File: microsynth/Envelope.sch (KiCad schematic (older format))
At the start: 42 parts, among them Q3 BC548, SW18-ENV-TO-VCF1 SW_SPDT, SW19-ENV-TO-VCO1 SW_SPDT, SW20-ENV-TO-KEYB1 SW_SPDT, SW7 SW_SPDT, SW8 SW_DPTT_SELECTOR-Switch, SW9 TRIGGER, U10 LM741, U3 4011, U4 4016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

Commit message: Change switch footprints
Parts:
- SW8, SW9: footprint Buttons_Switches_ThroughHole:DP3T_Toggle -> Buttons_Switches_ThroughHole:L203011MS02Q
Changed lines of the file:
@@
 F 0 "SW9" H 7900 4800 50  0000 L CNN
 F 1 "TRIGGER" H 7900 4700 50  0000 L CNN
-F 2 "Buttons_Switches_ThroughHole:DP3T_Toggle" H 7700 4800 50  0001 C CNN
+F 2 "Buttons_Switches_ThroughHole:L203011MS02Q" H 7700 4800 50  0001 C CNN
 F 3 "" H 7700 4800 50  0001 C CNN
 	1    7700 4800
@@
 F 0 "SW8" H 3200 3750 50  0000 L CNN
 F 1 "SW_DPTT_SELECTOR-Switch" H 3200 3650 50  0000 L CNN
-F 2 "Buttons_Switches_ThroughHole:DP3T_Toggle" H 2950 3550 50  0001 C CNN
+F 2 "Buttons_Switches_ThroughHole:L203011MS02Q" H 2950 3550 50  0001 C CNN
 F 3 "http://switches-connectors-custom.cwind.com/Asset/G-1128S-1110_2D%20DRAWING.pdf" H 2950 3550 50  0001 C CNN
 F 4 "Sustain" H 3200 3550 50  0000 L CNN "Label"
@@
 F 0 "SW8" H 3200 3650 50  0000 L CNN
 F 1 "SW_DPTT_SELECTOR-Switch" H 3200 3550 50  0000 L CNN
-F 2 "Buttons_Switches_ThroughHole:DP3T_Toggle" H 2950 3650 50  0001 C CNN
+F 2 "Buttons_Switches_ThroughHole:L203011MS02Q" H 2950 3650 50  0001 C CNN
 F 3 "http://switches-connectors-custom.cwind.com/Asset/G-1128S-1110_2D%20DRAWING.pdf" H 2950 3650 50  0001 C CNN
 	1    2950 3650

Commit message: Layout...-7
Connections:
- net +VSW: now also SW8.3; no longer SW8.7
- net TO_VCA_R136: now also SW8.4; no longer SW8.8
- net at R61.2, U4.5: now also SW8.6, SW8.8; no longer SW8.2, SW8.4
- net at U8.10, U8.12: now also SW8.7; no longer SW8.3
- net at C10.2, C9.2, D5.1 (K)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: now also SW8.5; no longer SW8.1
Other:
- moved on the sheet: SW8A, SW8B
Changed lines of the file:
@@
 L Switch:SW_DPTT_SELECTOR-Switch SW8
 U 2 1 5F2DFAB2
-P 2950 3550
-F 0 "SW8" H 3200 3750 50  0000 L CNN
-F 1 "SW_DPTT_SELECTOR-Switch" H 3200 3650 50  0000 L CNN
-F 2 "Buttons_Switches_ThroughHole:L203011MS02Q" H 2950 3550 50  0001 C CNN
-F 3 "http://switches-connectors-custom.cwind.com/Asset/G-1128S-1110_2D%20DRAWING.pdf" H 2950 3550 50  0001 C CNN
-F 4 "Sustain" H 3200 3550 50  0000 L CNN "Label"
-	2    2950 3550
-	1    0    0    -1
+P 2950 3650
+F 0 "SW8" H 3200 3850 50  0000 L CNN
+F 1 "SW_DPTT_SELECTOR-Switch" H 3200 3750 50  0000 L CNN
+F 2 "Buttons_Switches_ThroughHole:L203011MS02Q" H 2950 3650 50  0001 C CNN
+F 3 "http://switches-connectors-custom.cwind.com/Asset/G-1128S-1110_2D%20DRAWING.pdf" H 2950 3650 50  0001 C CNN
+F 4 "Sustain" H 3200 3650 50  0000 L CNN "Label"
+	2    2950 3650
+	1    0    0    1
 $EndComp
 $Comp
 L Switch:SW_DPTT_SELECTOR-Switch SW8
 U 1 1 5F2DEA06
-P 2950 3650
-F 0 "SW8" H 3200 3650 50  0000 L CNN
-F 1 "SW_DPTT_SELECTOR-Switch" H 3200 3550 50  0000 L CNN
-F 2 "Buttons_Switches_ThroughHole:L203011MS02Q" H 2950 3650 50  0001 C CNN
-F 3 "http://switches-connectors-custom.cwind.com/Asset/G-1128S-1110_2D%20DRAWING.pdf" H 2950 3650 50  0001 C CNN
-	1    2950 3650
-	1    0    0    -1
+P 2950 3550
+F 0 "SW8" H 3200 3550 50  0000 L CNN
+F 1 "SW_DPTT_SELECTOR-Switch" H 3200 3450 50  0000 L CNN
+F 2 "Buttons_Switches_ThroughHole:L203011MS02Q" H 2950 3550 50  0001 C CNN
+F 3 "http://switches-connectors-custom.cwind.com/Asset/G-1128S-1110_2D%20DRAWING.pdf" H 2950 3550 50  0001 C CNN
+	1    2950 3550
+	1    0    0    1
 $EndComp
 Wire Wire Line

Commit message: Layout...-3
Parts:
- SW8: value SW_DPTT_SELECTOR-Switch -> SUSTAIN
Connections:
- net +VSW: now also SW8.7; no longer SW8.3
- net TO_D3: now also SW9.6; no longer SW9.3
- net TO_VCA_R136: now also SW8.8; no longer SW8.4
- net at R61.2, U4.5: now also SW8.2, SW8.4; no longer SW8.6, SW8.8
- net at U8.10, U8.12: now also SW8.3; no longer SW8.7
- net at C10.2, C9.2, D5.1 (K)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: now also SW8.1; no longer SW8.5
- net at C13.2, U3.10, U3.12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: now also SW9.7; no longer SW9.2
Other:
- moved on the sheet: SW8A, SW8B
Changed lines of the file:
@@
 	8850 4300 8800 4300
 $Comp
-L power:-VSW #PWR0182
+L power:-VSW #PWR?
 U 1 1 5E64C648
 P 8850 4800
-F 0 "#PWR0182" H 8850 4900 50  0001 C CNN
+F 0 "#PWR?" H 8850 4900 50  0001 C CNN
 F 1 "-VSW" H 8865 4973 50  0000 C CNN
 F 2 "" H 8850 4800 50  0001 C CNN
@@
 $EndComp
 $Comp
-L power:GND #PWR0183
+L power:GND #PWR?
 U 1 1 5E652014
 P 5600 3600
-F 0 "#PWR0183" H 5600 3350 50  0001 C CNN
+F 0 "#PWR?" H 5600 3350 50  0001 C CNN
 F 1 "GND" H 5605 3427 50  0000 C CNN
 F 2 "" H 5600 3600 50  0001 C CNN
@@
 Connection ~ 6300 4250
 $Comp
-L power:GND #PWR0184
+L power:GND #PWR?
 U 1 1 5E65990E
 P 5600 5000
-F 0 "#PWR0184" H 5600 4750 50  0001 C CNN
+F 0 "#PWR?" H 5600 4750 50  0001 C CNN
 F 1 "GND" H 5605 4827 50  0000 C CNN
 F 2 "" H 5600 5000 50  0001 C CNN
@@
 	5600 4750 5650 4750
 $Comp
-L power:-VSW #PWR0185
+L power:-VSW #PWR?
 U 1 1 5E65BC6F
 P 6650 4900
-F 0 "#PWR0185" H 6650 5000 50  0001 C CNN
+F 0 "#PWR?" H 6650 5000 50  0001 C CNN
 F 1 "-VSW" H 6665 5073 50  0000 C CNN
 F 2 "" H 6650 4900 50  0001 C CNN
@@
 	1300 3100 1400 3100
 $Comp
-L power:-VSW #PWR0186
+L power:-VSW #PWR?
 U 1 1 5E66382E
 P 1300 3650
-F 0 "#PWR0186" H 1300 3750 50  0001 C CNN
+F 0 "#PWR?" H 1300 3750 50  0001 C CNN
 F 1 "-VSW" H 1315 3823 50  0000 C CNN
 F 2 "" H 1300 3650 50  0001 C CNN
@@
 	1300 3650 1300 3550
 $Comp
-L power:-VSW #PWR0187
+L power:-VSW #PWR?
 U 1 1 5E666239
 P 5150 5150
-F 0 "#PWR0187" H 5150 5250 50  0001 C CNN
+F 0 "#PWR?" H 5150 5250 50  0001 C CNN
 F 1 "-VSW" H 5165 5323 50  0000 C CNN
 F 2 "" H 5150 5150 50  0001 C CNN
@@
 	3850 3050 3850 3300
 $Comp
-L power:+VSW #PWR0188
+L power:+VSW #PWR?
 U 1 1 5E66EFC8
 P 4350 3050
-F 0 "#PWR0188" H 4350 2900 50  0001 C CNN
+F 0 "#PWR?" H 4350 2900 50  0001 C CNN
 F 1 "+VSW" H 4365 3223 50  0000 C CNN
 F 2 "" H 4350 3050 50  0001 C CNN
@@
 $EndComp
 $Comp
-L power:-VSW #PWR0189
+L power:-VSW #PWR?
 U 1 1 5E6A252E
 P 1300 2350
-F 0 "#PWR0189" H 1300 2450 50  0001 C CNN
+F 0 "#PWR?" H 1300 2450 50  0001 C CNN
 F 1 "-VSW" H 1315 2523 50  0000 C CNN
 F 2 "" H 1300 2350 50  0001 C CNN
@@
 $EndComp
 $Comp
-L power:-VSW #PWR0190
+L power:-VSW #PWR?
 U 1 1 5E6D9EA0
 P 3300 2100
-F 0 "#PWR0190" H 3300 2200 50  0001 C CNN
+F 0 "#PWR?" H 3300 2200 50  0001 C CNN
 F 1 "-VSW" H 3315 2273 50  0000 C CNN
 F 2 "" H 3300 2100 50  0001 C CNN
@@
 $EndComp
 $Comp
-L power:GND #PWR0191
+L power:GND #PWR?
 U 1 1 5E79E312
 P 9600 4000
-F 0 "#PWR0191" H 9600 3750 50  0001 C CNN
+F 0 "#PWR?" H 9600 3750 50  0001 C CNN
 F 1 "GND" H 9605 3827 50  0000 C CNN
 F 2 "" H 9600 4000 50  0001 C CNN
@@
 	8050 2500 7950 2500
 $Comp
-L power:-VSW #PWR0192
+L power:-VSW #PWR?
 U 1 1 5E8A19EA
 P 9000 2550
-F 0 "#PWR0192" H 9000 2650 50  0001 C CNN
+F 0 "#PWR?" H 9000 2650 50  0001 C CNN
 F 1 "-VSW" H 9015 2723 50  0000 C CNN
 F 2 "" H 9000 2550 50  0001 C CNN
@@
 $EndComp
 $Comp
-L power:+VSW #PWR0193
+L power:+VSW #PWR?
 U 1 1 5E8A24FD
 P 9000 1550
-F 0 "#PWR0193" H 9000 1400 50  0001 C CNN
+F 0 "#PWR?" H 9000 1400 50  0001 C CNN
 F 1 "+VSW" H 9015 1723 50  0000 C CNN
 F 2 "" H 9000 1550 50  0001 C CNN
@@
 $EndComp
 $Comp
-L power:+VSW #PWR0194
+L power:+VSW #PWR?
 U 1 1 5E8A2FBB
 P 9650 1550
-F 0 "#PWR0194" H 9650 1400 50  0001 C CNN
+F 0 "#PWR?" H 9650 1400 50  0001 C CNN
 F 1 "+VSW" H 9665 1723 50  0000 C CNN
 F 2 "" H 9650 1550 50  0001 C CNN
@@
 	700  850  700  2850
 $Comp
-L power:-VSW #PWR0196
+L power:-VSW #PWR?
 U 1 1 5E8BB478
 P 5850 2950
-F 0 "#PWR0196" H 5850 3050 50  0001 C CNN
+F 0 "#PWR?" H 5850 3050 50  0001 C CNN
 F 1 "-VSW" H 5865 3123 50  0000 C CNN
 F 2 "" H 5850 2950 50  0001 C CNN
@@
 $EndComp
 $Comp
-L power:+VSW #PWR0197
+L power:+VSW #PWR?
 U 1 1 5E8BBF3F
 P 5850 3550
-F 0 "#PWR0197" H 5850 3400 50  0001 C CNN
+F 0 "#PWR?" H 5850 3400 50  0001 C CNN
 F 1 "+VSW" H 5865 3723 50  0000 C CNN
 F 2 "" H 5850 3550 50  0001 C CNN
@@
 $EndComp
 $Comp
-L power:-VSW #PWR0198
+L power:-VSW #PWR?
 U 1 1 5E8BD7DD
 P 5850 4350
-F 0 "#PWR0198" H 5850 4450 50  0001 C CNN
+F 0 "#PWR?" H 5850 4450 50  0001 C CNN
 F 1 "-VSW" H 5865 4523 50  0000 C CNN
 F 2 "" H 5850 4350 50  0001 C CNN
@@
 $EndComp
 $Comp
-L power:+VSW #PWR0199
+L power:+VSW #PWR?
 U 1 1 5E8BE2B0
 P 5850 4950
-F 0 "#PWR0199" H 5850 4800 50  0001 C CNN
+F 0 "#PWR?" H 5850 4800 50  0001 C CNN
 F 1 "+VSW" H 5865 5123 50  0000 C CNN
 F 2 "" H 5850 4950 50  0001 C CNN
@@
 $Comp
 L microsynth-rescue:SW_DPTT_SELECTOR-Switch SW9
-U 1 1 5E95BE3D
+U 2 1 5E95BE3D
 P 7700 4800
 F 0 "SW9" H 7900 4800 50  0000 L CNN
@@
 F 2 "Buttons_Switches_ThroughHole:L203011MS02Q" H 7700 4800 50  0001 C CNN
 F 3 "" H 7700 4800 50  0001 C CNN
-	1    7700 4800
-	1    0    0    -1
+	2    7700 4800
+	-1   0    0    1
 $EndComp
 $Comp
@@
 $EndComp
 $Comp
-L power:-VSW #PWR0195
+L power:-VSW #PWR?
 U 1 1 5E8A3AFC
 P 9650 2550
-F 0 "#PWR0195" H 9650 2650 50  0001 C CNN
+F 0 "#PWR?" H 9650 2650 50  0001 C CNN
 F 1 "-VSW" H 9665 2723 50  0000 C CNN
 F 2 "" H 9650 2550 50  0001 C CNN
@@
 $EndComp
 $Comp
-L power:-VSW #PWR0149
+L power:-VSW #PWR?
 U 1 1 5EC0045E
 P 10350 2550
-F 0 "#PWR0149" H 10350 2650 50  0001 C CNN
+F 0 "#PWR?" H 10350 2650 50  0001 C CNN
 F 1 "-VSW" H 10365 2723 50  0000 C CNN
 F 2 "" H 10350 2550 50  0001 C CNN
@@
 $EndComp
 $Comp
-L power:+VSW #PWR0150
+L power:+VSW #PWR?
 U 1 1 5EC00B84
 P 10350 1550
-F 0 "#PWR0150" H 10350 1400 50  0001 C CNN
+F 0 "#PWR?" H 10350 1400 50  0001 C CNN
 F 1 "+VSW" H 10365 1723 50  0000 C CNN
 F 2 "" H 10350 1550 50  0001 C CNN
@@
 L Switch:SW_DPTT_SELECTOR-Switch SW8
 U 2 1 5F2DFAB2
+P 2950 3550
+F 0 "SW8" H 3200 3750 50  0000 L CNN
+F 1 "SUSTAIN" H 3200 3650 50  0000 L CNN
+F 2 "Buttons_Switches_ThroughHole:L203011MS02Q" H 2950 3550 50  0001 C CNN
+F 3 "http://switches-connectors-custom.cwind.com/Asset/G-1128S-1110_2D%20DRAWING.pdf" H 2950 3550 50  0001 C CNN
+F 4 "Sustain" H 3200 3550 50  0001 L CNN "Label"
+	2    2950 3550
+	1    0    0    -1
+$EndComp
+$Comp
+L Switch:SW_DPTT_SELECTOR-Switch SW8
+U 1 1 5F2DEA06
 P 2950 3650
-F 0 "SW8" H 3200 3850 50  0000 L CNN
-F 1 "SW_DPTT_SELECTOR-Switch" H 3200 3750 50  0000 L CNN
+F 0 "SW8" H 3200 3650 50  0000 L CNN
+F 1 "SUSTAIN" H 3200 3550 50  0000 L CNN
 F 2 "Buttons_Switches_ThroughHole:L203011MS02Q" H 2950 3650 50  0001 C CNN
 F 3 "http://switches-connectors-custom.cwind.com/Asset/G-1128S-1110_2D%20DRAWING.pdf" H 2950 3650 50  0001 C CNN
-F 4 "Sustain" H 3200 3650 50  0000 L CNN "Label"
-	2    2950 3650
-	1    0    0    1
-$EndComp
-$Comp
-L Switch:SW_DPTT_SELECTOR-Switch SW8
-U 1 1 5F2DEA06
-P 2950 3550
-F 0 "SW8" H 3200 3550 50  0000 L CNN
-F 1 "SW_DPTT_SELECTOR-Switch" H 3200 3450 50  0000 L CNN
-F 2 "Buttons_Switches_ThroughHole:L203011MS02Q" H 2950 3550 50  0001 C CNN
-F 3 "http://switches-connectors-custom.cwind.com/Asset/G-1128S-1110_2D%20DRAWING.pdf" H 2950 3550 50  0001 C CNN
-	1    2950 3550
-	1    0    0    1
-$EndComp
-Wire Wire Line
+	1    2950 3650
+	1    0    0    -1
+$EndComp
+Wire Wire Line

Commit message: Tidy up, name switches, proper footprints for all trimmers
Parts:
- SW18-ENV-TO-VCF1, SW19-ENV-TO-VCO1, SW20-ENV-TO-KEYB1, SW7: footprint 4ms:SPDT_KIT -> Buttons_Switches_ThroughHole:GF-624-6014
- SW8, SW9: footprint Buttons_Switches_ThroughHole:L203011MS02Q -> Buttons_Switches_ThroughHole:G-1128S-1110
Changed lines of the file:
@@
 F 0 "SW7" V 3859 1712 50  0000 R CNN
 F 1 "SW_SPDT" V 3950 1712 50  0000 R CNN
-F 2 "4ms:SPDT_KIT" H 3950 1900 50  0001 C CNN
+F 2 "Buttons_Switches_ThroughHole:GF-624-6014" H 3950 1900 50  0001 C CNN
 F 3 "~" H 3950 1900 50  0001 C CNN
 F 4 "ADSR" V 4041 1712 50  0000 R CNN "Label"
@@
 F 0 "SW19-ENV-TO-VCO1" H 7750 1985 50  0000 C CNN
 F 1 "SW_SPDT" H 7750 1894 50  0000 C CNN
-F 2 "4ms:SPDT_KIT" H 7750 1700 50  0001 C CNN
+F 2 "Buttons_Switches_ThroughHole:GF-624-6014" H 7750 1700 50  0001 C CNN
 F 3 "~" H 7750 1700 50  0001 C CNN
 	1    7750 1700
@@
 F 0 "SW18-ENV-TO-VCF1" H 7750 2685 50  0000 C CNN
 F 1 "SW_SPDT" H 7750 2594 50  0000 C CNN
-F 2 "4ms:SPDT_KIT" H 7750 2400 50  0001 C CNN
+F 2 "Buttons_Switches_ThroughHole:GF-624-6014" H 7750 2400 50  0001 C CNN
 F 3 "~" H 7750 2400 50  0001 C CNN
 	1    7750 2400
@@
 F 0 "SW9" H 7900 4800 50  0000 L CNN
 F 1 "TRIGGER" H 7900 4700 50  0000 L CNN
-F 2 "Buttons_Switches_ThroughHole:L203011MS02Q" H 7700 4800 50  0001 C CNN
+F 2 "Buttons_Switches_ThroughHole:G-1128S-1110" H 7700 4800 50  0001 C CNN
 F 3 "" H 7700 4800 50  0001 C CNN
 	2    7700 4800
@@
 F 0 "SW20-ENV-TO-KEYB1" H 7750 1285 50  0000 C CNN
 F 1 "SW_SPDT" H 7750 1194 50  0000 C CNN
-F 2 "4ms:SPDT_KIT" H 7750 1000 50  0001 C CNN
+F 2 "Buttons_Switches_ThroughHole:GF-624-6014" H 7750 1000 50  0001 C CNN
 F 3 "~" H 7750 1000 50  0001 C CNN
 	1    7750 1000
@@
 F 0 "SW8" H 3200 3750 50  0000 L CNN
 F 1 "SUSTAIN" H 3200 3650 50  0000 L CNN
-F 2 "Buttons_Switches_ThroughHole:L203011MS02Q" H 2950 3550 50  0001 C CNN
+F 2 "Buttons_Switches_ThroughHole:G-1128S-1110" H 2950 3550 50  0001 C CNN
 F 3 "http://switches-connectors-custom.cwind.com/Asset/G-1128S-1110_2D%20DRAWING.pdf" H 2950 3550 50  0001 C CNN
 F 4 "Sustain" H 3200 3550 50  0001 L CNN "Label"
@@
 F 0 "SW8" H 3200 3650 50  0000 L CNN
 F 1 "SUSTAIN" H 3200 3550 50  0000 L CNN
-F 2 "Buttons_Switches_ThroughHole:L203011MS02Q" H 2950 3650 50  0001 C CNN
+F 2 "Buttons_Switches_ThroughHole:G-1128S-1110" H 2950 3650 50  0001 C CNN
 F 3 "http://switches-connectors-custom.cwind.com/Asset/G-1128S-1110_2D%20DRAWING.pdf" H 2950 3650 50  0001 C CNN
 	1    2950 3650

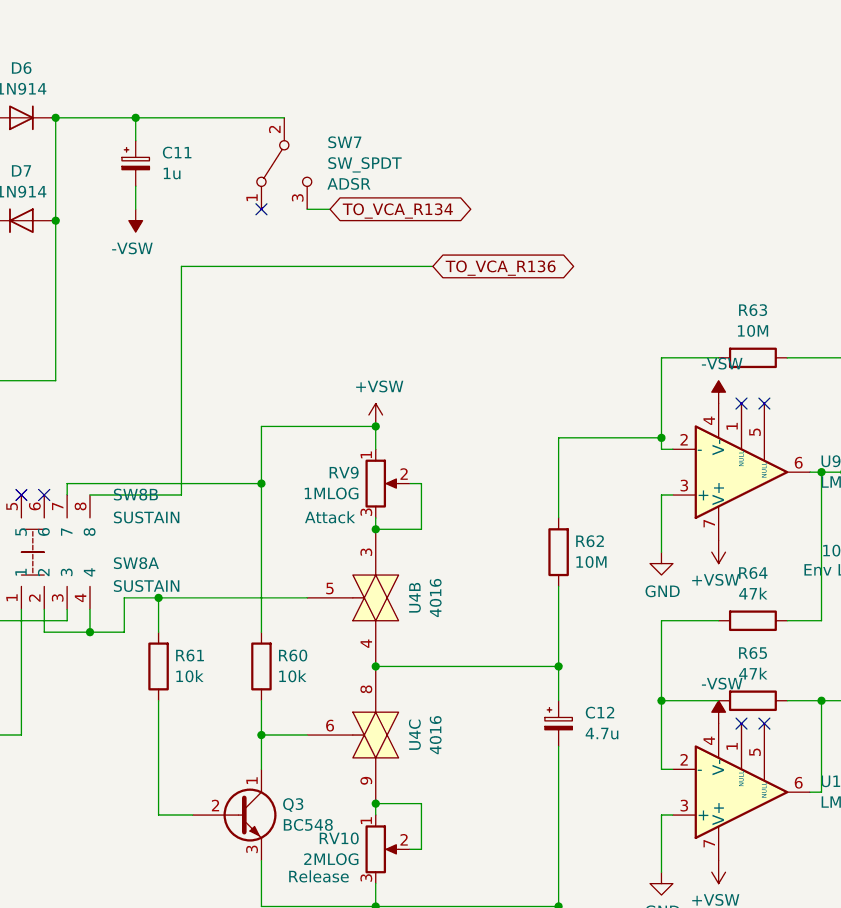
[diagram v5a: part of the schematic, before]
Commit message: Proper capacitor footprints
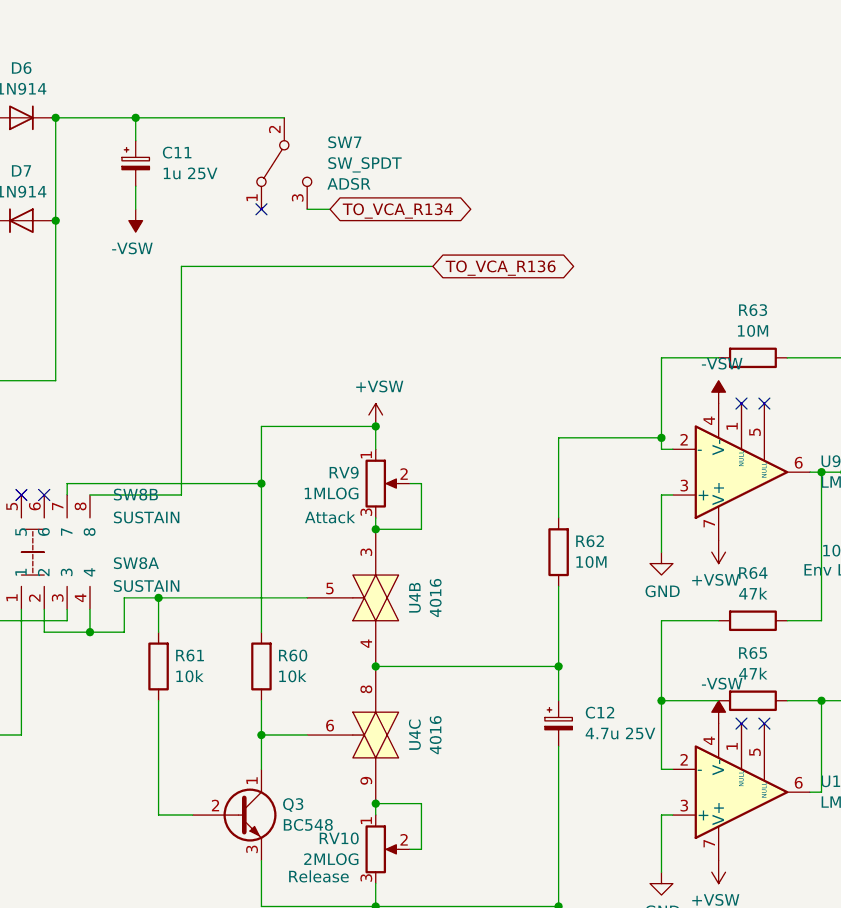
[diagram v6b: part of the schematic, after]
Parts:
- C10, C13, C14, C9: footprint Capacitor_THT:C_Disc_D5.0mm_W2.5mm_P5.00mm -> Capacitor_THT:C_Rect_L7.2mm_W2.5mm_P5.00mm_FKS2_FKP2_MKS2_MKP2
- C11: value 1u -> 1u 25V
- C12: value 4.7u -> 4.7u 25V
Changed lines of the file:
@@
 F 0 "C9" V 798 1850 50  0000 C CNN
 F 1 "10n" V 889 1850 50  0000 C CNN
-F 2 "Capacitor_THT:C_Disc_D5.0mm_W2.5mm_P5.00mm" H 1088 1700 50  0001 C CNN
+F 2 "Capacitor_THT:C_Rect_L7.2mm_W2.5mm_P5.00mm_FKS2_FKP2_MKS2_MKP2" H 1088 1700 50  0001 C CNN
 F 3 "~" H 1050 1850 50  0001 C CNN
 	1    1050 1850
@@
 F 0 "C10" V 798 3100 50  0000 C CNN
 F 1 "10n" V 889 3100 50  0000 C CNN
-F 2 "Capacitor_THT:C_Disc_D5.0mm_W2.5mm_P5.00mm" H 1088 2950 50  0001 C CNN
+F 2 "Capacitor_THT:C_Rect_L7.2mm_W2.5mm_P5.00mm_FKS2_FKP2_MKS2_MKP2" H 1088 2950 50  0001 C CNN
 F 3 "~" H 1050 3100 50  0001 C CNN
 	1    1050 3100
@@
 F 0 "C13" V 8398 4300 50  0000 C CNN
 F 1 "10n" V 8489 4300 50  0000 C CNN
-F 2 "Capacitor_THT:C_Disc_D5.0mm_W2.5mm_P5.00mm" H 8688 4150 50  0001 C CNN
+F 2 "Capacitor_THT:C_Rect_L7.2mm_W2.5mm_P5.00mm_FKS2_FKP2_MKS2_MKP2" H 8688 4150 50  0001 C CNN
 F 3 "~" H 8650 4300 50  0001 C CNN
 	1    8650 4300
@@
 P 5150 4350
 F 0 "C12" H 5265 4396 50  0000 L CNN
-F 1 "4.7u" H 5265 4305 50  0000 L CNN
+F 1 "4.7u 25V" H 5265 4305 50  0000 L CNN
 F 2 "Capacitor_THT:CP_Radial_D5.0mm_P2.50mm" H 5188 4200 50  0001 C CNN
 F 3 "~" H 5150 4350 50  0001 C CNN
@@
 P 3300 1900
 F 0 "C11" H 3415 1946 50  0000 L CNN
-F 1 "1u" H 3415 1855 50  0000 L CNN
+F 1 "1u 25V" H 3415 1855 50  0000 L CNN
 F 2 "Capacitor_THT:CP_Radial_D5.0mm_P2.50mm" H 3338 1750 50  0001 C CNN
 F 3 "~" H 3300 1900 50  0001 C CNN
@@
 F 0 "C14" H 9715 3896 50  0000 L CNN
 F 1 "100n" H 9715 3805 50  0000 L CNN
-F 2 "Capacitor_THT:C_Disc_D5.0mm_W2.5mm_P5.00mm" H 9638 3700 50  0001 C CNN
+F 2 "Capacitor_THT:C_Rect_L7.2mm_W2.5mm_P5.00mm_FKS2_FKP2_MKS2_MKP2" H 9638 3700 50  0001 C CNN
 F 3 "~" H 9600 3850 50  0001 C CNN
 	1    9600 3850
